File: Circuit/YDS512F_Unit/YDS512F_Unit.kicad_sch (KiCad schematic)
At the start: 2 parts, among them J1 Conn_01x07_Pin, U1 YDS512F

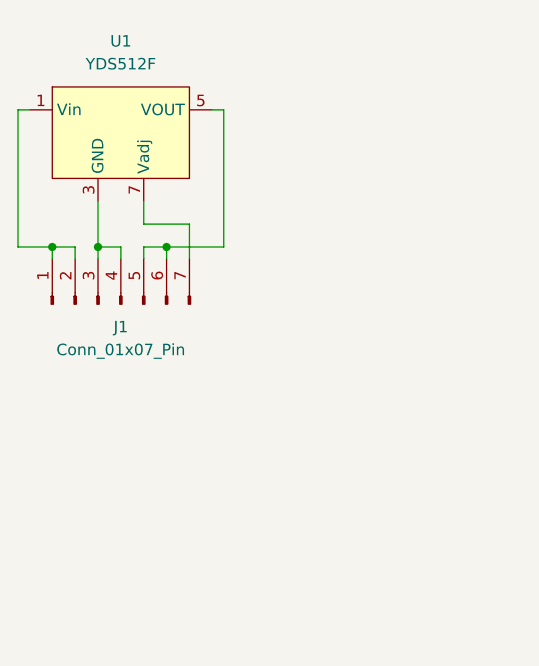
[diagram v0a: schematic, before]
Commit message: YDS512F基板完成 24V基板とメインモータ基板を微修正
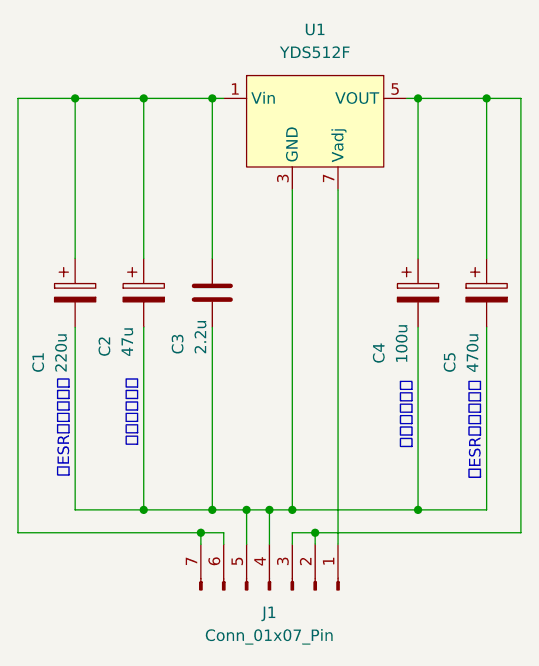
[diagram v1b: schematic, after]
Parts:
- added C1: 220u, Capacitor_THT:CP_Radial_D10.0mm_P5.00mm, symbol Device:C_Polarized
- added C2: 47u, Capacitor_THT:CP_Radial_D8.0mm_P3.50mm, symbol Device:C_Polarized
- added C3: 2.2u, Capacitor_THT:C_Disc_D6.0mm_W4.4mm_P5.00mm, symbol Device:C
- added C4: 100u, Capacitor_THT:CP_Radial_D10.0mm_P5.00mm, symbol Device:C_Polarized
- added C5: 470u, Capacitor_THT:CP_Radial_D10.0mm_P5.00mm, symbol Device:C_Polarized
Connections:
- net at U1.1 (Vin), U1.2 (Vin): now also J1.6 (Pin_6), J1.7 (Pin_7), C1.1, C2.1, C3.1; no longer J1.1 (Pin_1), J1.2 (Pin_2)
- net at J1.4 (Pin_4), U1.3 (GND), U1.4 (GND): now also J1.5 (Pin_5), C1.2, C2.2, C3.2, C4.2, C5.2; no longer J1.3 (Pin_3)
- net at U1.5 (VOUT), U1.6 (VOUT): now also J1.2 (Pin_2), J1.3 (Pin_3), C4.1, C5.1; no longer J1.5 (Pin_5), J1.6 (Pin_6)
- net at U1.7 (Vadj): now also J1.1 (Pin_1); no longer J1.7 (Pin_7)
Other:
- note added: "低ESRアルミ電解"
- note added: "導電性高分子"
- moved on the sheet: J1, U1

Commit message: 発注用データを用意 発注した
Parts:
- J1: MPN_URL (none) -> https://akizukidenshi.com/catalog/g/g101627/
- U1: MPN_URL (none) -> https://akizukidenshi.com/catalog/g/g116702/
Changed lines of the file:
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@@
+			)
+		)
+		(property "MPN_URL" "https://akizukidenshi.com/catalog/g/g101627/"
+			(at 48.26 80.01 90)
+			(hide yes)
+			(show_name no)
+			(do_not_autoplace no)
+			(effects
+				(font
+					(size 1.27 1.27)
+				)
 			)
 		)
@@
 			(at 53.34 27.94 0)
 			(hide yes)
+			(show_name no)
+			(do_not_autoplace no)
+			(effects
+				(font
+					(size 1.27 1.27)
+				)
+			)
+		)
+		(property "MPN_URL" "https://akizukidenshi.com/catalog/g/g116702/"
+			(at 53.34 27.94 0)
+			(hide yes)
